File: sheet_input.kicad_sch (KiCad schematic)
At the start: 48 parts, among them J1 NCJ6FA-H, J5 VDD_PoE / PGND, J7 TO EURORACK MODULE (alt. to J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, K1 KAQY214S, K2 KAQY214S, Q1 DMP3098 (P-FET 60V), SW1 SS-12D00-G3, U3 TLV9061, U4 74HC4053

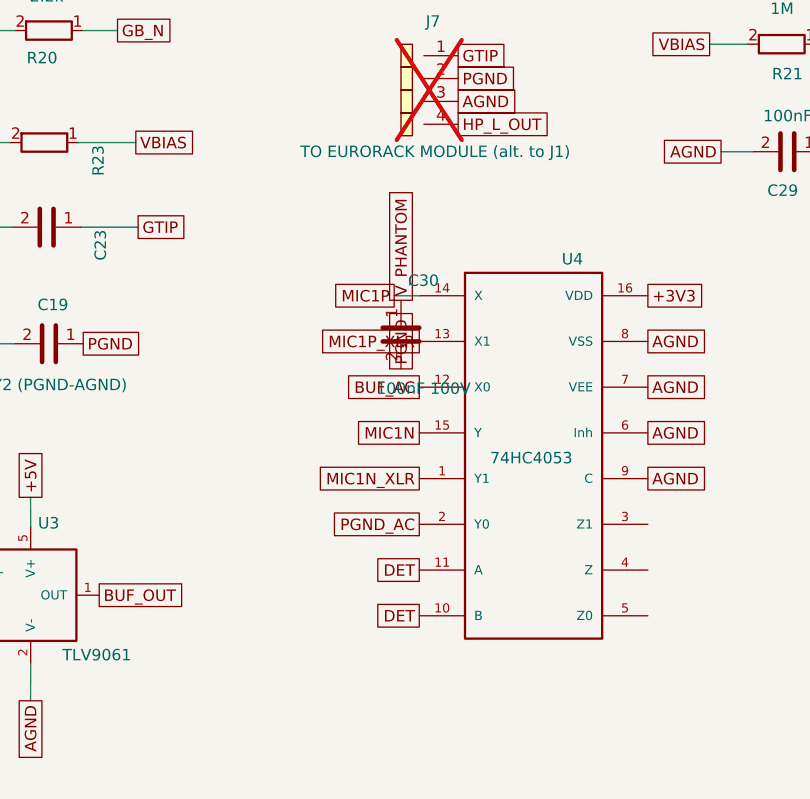
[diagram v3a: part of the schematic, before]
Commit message: pcb: input-corridor tweaks; J6 display header now DNP; regen fab + docs
- J6 hand-fit per build; eurorack builds don't need it at all (the
  Synthia interposer drives the display directly from its own socket)
- BOM: J6 marked DNP; fab assembly split updated (JLC THT = J3/J4 only;
  CPL 69 placed, 9 exclusions: C19 J1 J2 J5 J6 J7 R14 R27 SW1)
- restore exclude_from_pos flags wiped by layout sessions
- README: power/host notes (USB-C + PoE concurrency, hot-plug pop,
  USB-only bench), brackets/ and docs/ in repo layout
- regen gerbers/BOM/CPL, doc PDFs, board STEP
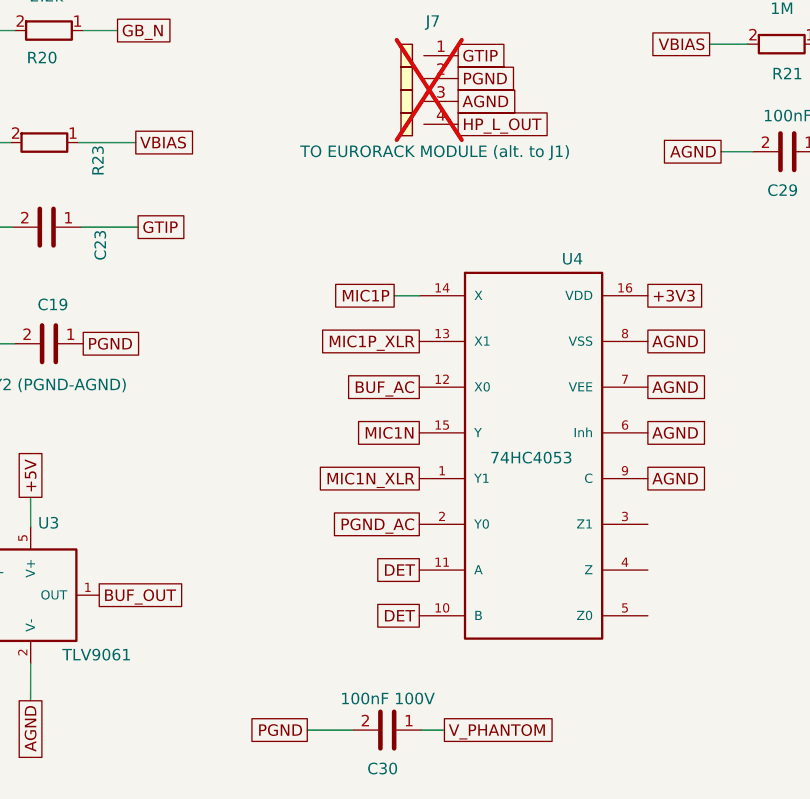
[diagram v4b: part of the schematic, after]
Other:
- moved on the sheet: C30
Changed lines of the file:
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@@
 		(comment 1 "Chunk 2: Neutrik combo input + ESD + isolated phantom block + isolation barrier + status LED")
 	)
-		(symbol
-			(lib_id "scramble_hat:C")
-			(at 340.36 179.07 0)
-			(unit 1)
-			(exclude_from_sim no)
-			(in_bom yes)
-			(on_board yes)
-			(dnp no)
-			(property "Reference" "C30"
-				(at 342.86 173.07 0)
-				(show_name no)
-				(do_not_autoplace no)
-				(effects (font (size 1.27 1.27)))
-			)
-			(property "Value" "100nF 100V"
-				(at 342.86 185.07 0)
-				(show_name no)
-				(do_not_autoplace no)
-				(effects (font (size 1.27 1.27)))
-			)
-			(property "Footprint" "Capacitor_SMD:C_0805_2012Metric"
-				(at 340.36 179.07 0)
-				(show_name no)
-				(do_not_autoplace no)
-				(hide yes)
-				(effects (font (size 1.27 1.27)))
-			)
-			(property "Datasheet" "https://datasheet.lcsc.com/datasheet/pdf/9f6ef17093b8d551f8b17af0626ff758.pdf?productCode=C89258"
-				(at 340.36 179.07 0)
-				(show_name no)
-				(do_not_autoplace no)
-				(hide yes)
-				(effects (font (size 1.27 1.27)))
-			)
-			(property "Description" "V_PHANTOM bypass at Q1 drain (PoE hash filter)"
-				(at 340.36 179.07 0)
-				(show_name no)
-				(do_not_autoplace no)
-				(hide yes)
-				(effects (font (size 1.27 1.27)))
-			)
-			(pin "1"
-			)
-			(pin "2"
-			)
-			(instances
-				(project "scramble_hat"
-					(path "/2b93e89d-bdf9-4578-8fa1-59d0c819a910/f89707d4-5ec9-426f-a042-e33ce0e25fbe"
-						(reference "C30")
-						(unit 1)
-					)
-				)
-			)
-		)
-	(global_label "V_PHANTOM"
-		(shape passive)
-		(at 340.36 175.26 90)
-		(effects
-			(font
-				(size 1.27 1.27)
-			)
-			(justify left)
-		)
-		(property "Intersheetrefs" "${INTERSHEET_REFS}"
-			(at 340.36 175.26 90)
-			(hide yes)
-			(show_name no)
-			(do_not_autoplace no)
-			(effects
-				(font
-					(size 1.27 1.27)
-				)
-			)
-		)
-	)
-	(global_label "PGND"
-		(shape passive)
-		(at 340.36 182.88 270)
-		(effects
-			(font
-				(size 1.27 1.27)
-			)
-			(justify left)
+	(wire
+		(pts
+			(xy 251.206 66.04) (xy 246.888 66.04)
 		)
-		(property "Intersheetrefs" "${INTERSHEET_REFS}"
-			(at 340.36 182.88 270)
-			(hide yes)
-			(show_name no)
-			(do_not_autoplace no)
-			(effects
-				(font
-					(size 1.27 1.27)
-				)
-			)
+		(stroke
+			(width 0)
+			(type default)
 		)
 	)
 	(wire
 		(pts
-			(xy 251.206 66.04) (xy 246.888 66.04)
+			(xy 329.946 223.012) (xy 335.026 223.012)
 		)
 		(stroke
@@
 	(wire
 		(pts
+			(xy 345.186 223.012) (xy 342.646 223.012)
+		)
+		(stroke
+			(width 0)
+			(type default)
+		)
+	)
+	(wire
+		(pts
 			(xy 185.928 118.364) (xy 183.5 118.364)
 		)
@@
 		)
 	)
+	(global_label "V_PHANTOM"
+		(shape passive)
+		(at 345.186 223.012 0)
+		(effects
+			(font
+				(size 1.27 1.27)
+			)
+			(justify left)
+		)
+		(property "Intersheetrefs" "${INTERSHEET_REFS}"
+			(at 345.186 223.012 0)
+			(hide yes)
+			(show_name no)
+			(do_not_autoplace no)
+			(effects
+				(font
+					(size 1.27 1.27)
+				)
+			)
+		)
+	)
 	(global_label "DET"
 		(shape passive)
@@
 		)
 	)
+	(global_label "PGND"
+		(shape passive)
+		(at 329.946 223.012 180)
+		(effects
+			(font
+				(size 1.27 1.27)
+			)
+			(justify right)
+		)
+		(property "Intersheetrefs" "${INTERSHEET_REFS}"
+			(at 329.946 223.012 0)
+			(hide yes)
+			(show_name no)
+			(do_not_autoplace no)
+			(effects
+				(font
+					(size 1.27 1.27)
+				)
+			)
+		)
+	)
 	(global_label "AGND"
 		(shape passive)
@@
 					(unit 1)
 				)
+			)
+		)
+	)
+	(symbol
+		(lib_id "scramble_hat:C")
+		(at 338.836 223.012 270)
+		(unit 1)
+		(body_style 1)
+		(exclude_from_sim no)
+		(in_bom yes)
+		(on_board yes)
+		(in_pos_files yes)
+		(dnp no)
+		(property "Reference" "C30"
+			(at 338.328 227.33 90)
+			(show_name no)
+			(do_not_autoplace no)
+			(effects
+				(font
+					(size 1.27 1.27)
+				)
+			)
+		)
+		(property "Value" "100nF 100V"
+			(at 338.876 219.552 90)
+			(show_name no)
+			(do_not_autoplace no)
+			(effects
+				(font
+					(size 1.27 1.27)
+				)
+			)
+		)
+		(property "Footprint" "Capacitor_SMD:C_0805_2012Metric"
+			(at 338.836 223.012 0)
+			(hide yes)
+			(show_name no)
+			(do_not_autoplace no)
+			(effects
+				(font
+					(size 1.27 1.27)
+				)
+			)
+		)
+		(property "Datasheet" "https://datasheet.lcsc.com/datasheet/pdf/9f6ef17093b8d551f8b17af0626ff758.pdf?productCode=C89258"
+			(at 338.836 223.012 0)
+			(hide yes)
+			(show_name no)
+			(do_not_autoplace no)
+			(effects
+				(font
+					(size 1.27 1.27)
+				)
+			)
+		)
+		(property "Description" "V_PHANTOM bypass at Q1 drain (PoE hash filter)"
+			(at 338.836 223.012 0)
+			(hide yes)
+			(show_name no)
+			(do_not_autoplace no)
+			(effects
+				(font
+					(size 1.27 1.27)
+				)
+			)
+		)
+		(pin "1"
+		)
+		(pin "2"
+		)
+		(instances
+			(project "scramble_hat"
+				(path "/2b93e89d-bdf9-4578-8fa1-59d0c819a910/f89707d4-5ec9-426f-a042-e33ce0e25fbe"
+					(reference "C30")
+					(unit 1)
+				)
